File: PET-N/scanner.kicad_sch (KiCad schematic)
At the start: 15 parts, among them J4 AVR-ISP-6, U2 ATmega32A-A, U3 74HCT85, U4 74LS174, U6 74LS174, U7 74LS145, Y1 ASE-xxxMHz

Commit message: layout work
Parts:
- added D80: 1N4448, Diode_SMD:D_SOD-323_HandSoldering, symbol PCM_Diode_AKL:1N4448
- added R4: 10k, Resistor_SMD:R_0603_1608Metric, symbol Device:R
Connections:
- net VCC: now also R4.2
- net /RESSCAN: now also D80.1 (K); no longer D78.2 (A), U2.4 (~{RESET})
- new net: D78.2 (A), D80.2 (A), R4.1, U2.4 (~{RESET})
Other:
- moved on the sheet: D78

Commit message: add orientation marker for backlight LEDs and move to 3.1B
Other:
- note added: "CBM-KEYB-PETN-3.1B-20260405"
- note removed: "CBM-KEYB-PETN-3.1A-20260130"
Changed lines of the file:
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@@
 		)
 	)
-	(text "CBM-KEYB-PETN-3.1A-20260130"
+	(text "CBM-KEYB-PETN-3.1B-20260405"
 		(exclude_from_sim no)
 		(at 231.14 175.26 0)

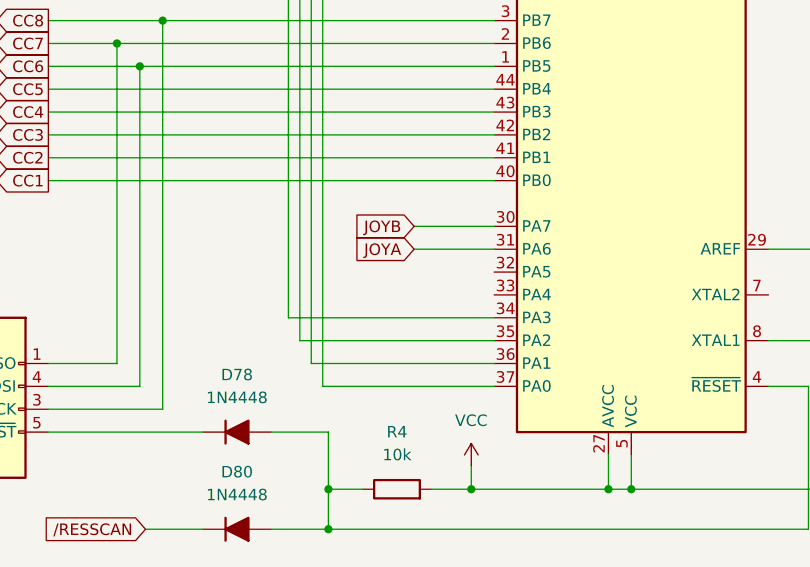
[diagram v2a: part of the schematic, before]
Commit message: add irq/nmi out
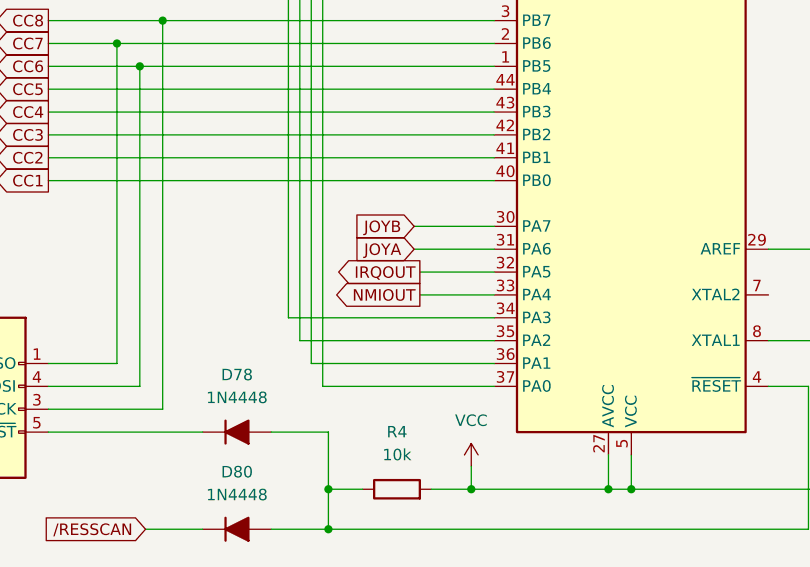
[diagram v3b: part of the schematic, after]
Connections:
- net IRQOUT: now reaches U2.32 (PA5)
- net NMIOUT: now reaches U2.33 (PA4)
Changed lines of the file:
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@@
+	(wire
+		(pts
+			(xy 225.425 132.715) (xy 233.68 132.715)
+		)
+		(stroke
+			(width 0)
+			(type default)
+		)
+	)
 	(wire
 		(pts
@@
 		(pts
 			(xy 233.68 71.755) (xy 185.42 71.755)
+		)
+		(stroke
+			(width 0)
+			(type default)
+		)
+	)
+	(wire
+		(pts
+			(xy 225.425 130.175) (xy 233.68 130.175)
 		)
 		(stroke
@@
 			(effects
 				(font
+					(size 1.27 1.27)
+				)
+				(justify right)
+				(hide yes)
+			)
+		)
+	)
+	(global_label "IRQOUT"
+		(shape output)
+		(at 225.425 130.175 180)
+		(fields_autoplaced yes)
+		(effects
+			(font
+				(size 1.27 1.27)
+			)
+			(justify right)
+		)
+		(property "Intersheetrefs" "${INTERSHEET_REFS}"
+			(at 216.2601 130.175 0)
+			(effects
+				(font
+					(size 1.27 1.27)
+				)
+				(justify right)
+				(hide yes)
+			)
+		)
+	)
+	(global_label "NMIOUT"
+		(shape output)
+		(at 225.425 132.715 180)
+		(fields_autoplaced yes)
+		(effects
+			(font
+				(size 1.27 1.27)
+			)
+			(justify right)
+		)
+		(property "Intersheetrefs" "${INTERSHEET_REFS}"
+			(at 216.0787 132.715 0)
+			(effects
+				(font
